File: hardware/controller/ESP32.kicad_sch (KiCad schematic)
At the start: 22 parts, among them J4 Conn_01x04_Pin, Q1 SS8050-G, Q2 SS8050-G, U2 ESP32-S3, Y1 FH4000074Z

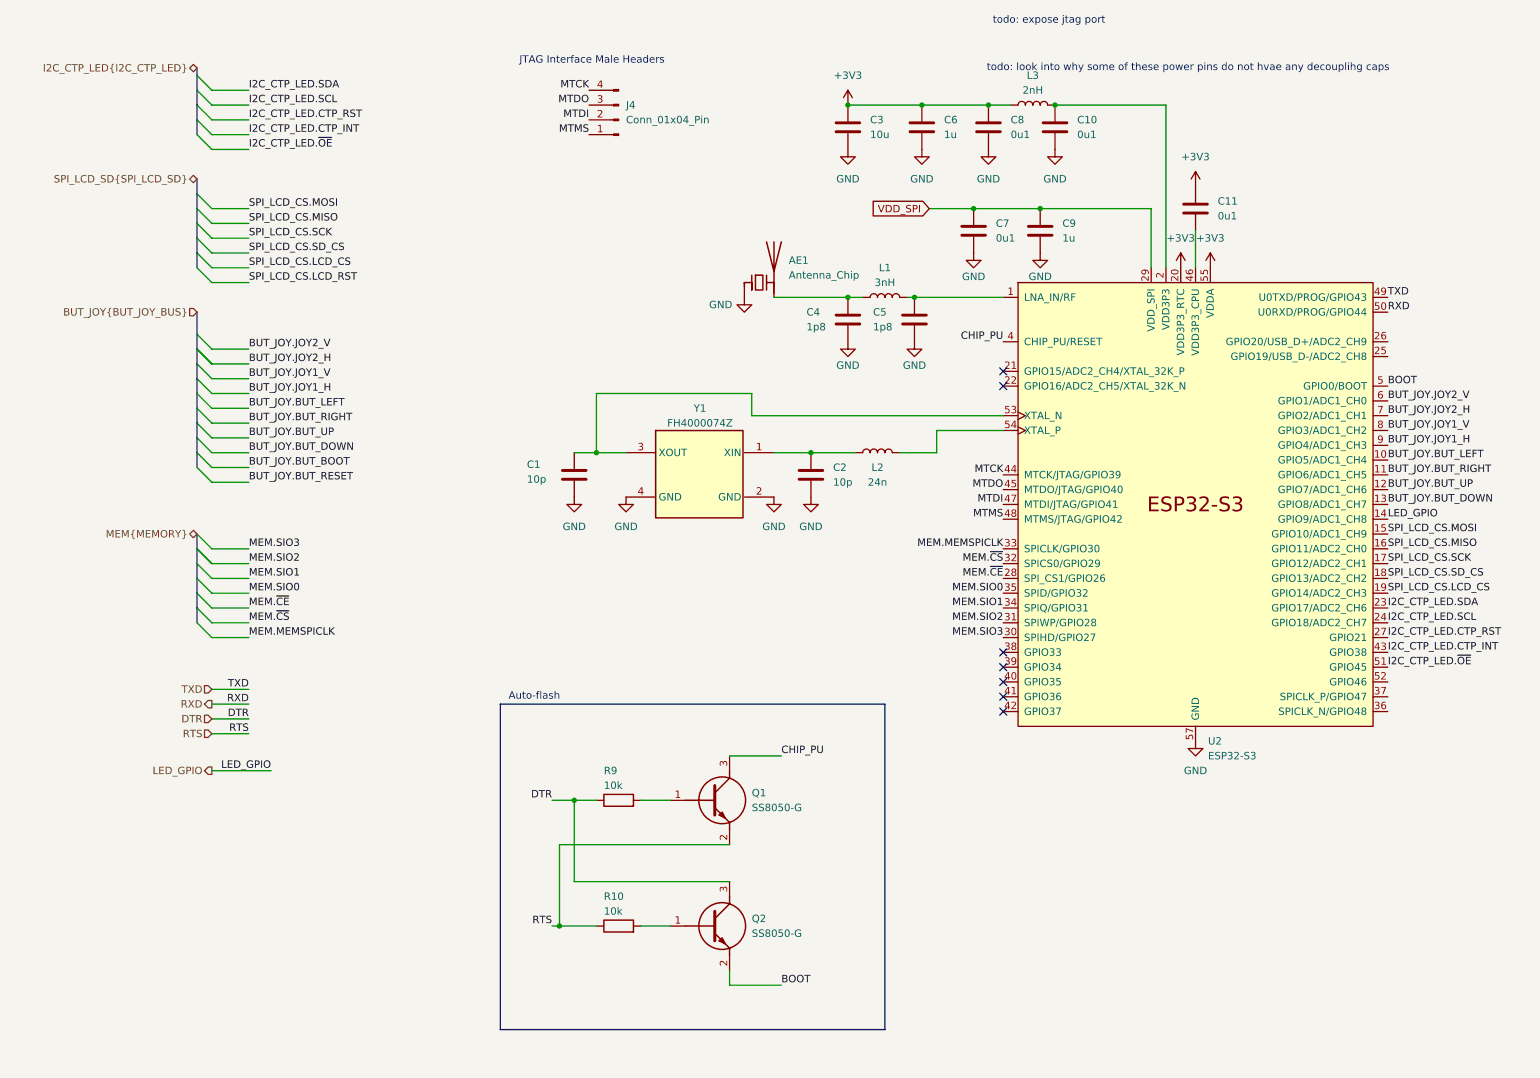
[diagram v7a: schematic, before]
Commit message: modified power circuitry
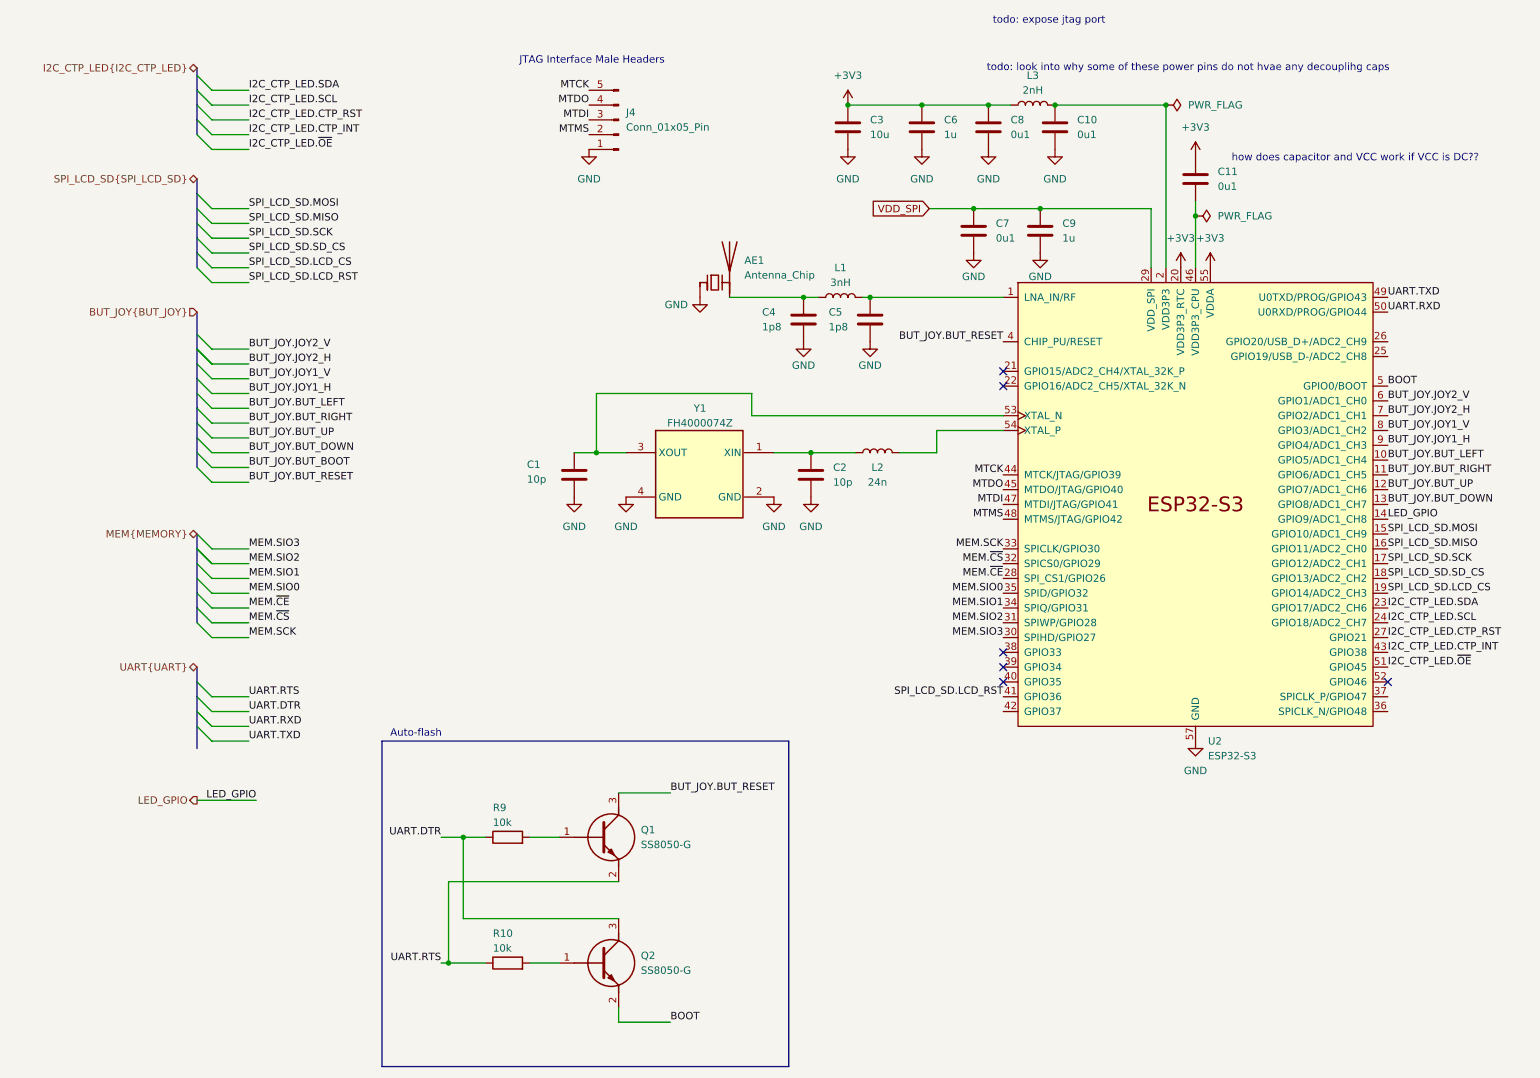
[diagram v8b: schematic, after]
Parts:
- AE1: footprint (none) -> RF_Antenna:Texas_SWRA117D_2.4GHz_Right
- J4: value Conn_01x04_Pin -> Conn_01x05_Pin; footprint (none) -> Connector_PinHeader_2.54mm:PinHeader_1x04_P2.54mm_Vertical; symbol Connector:Conn_01x04_Pin -> Connector:Conn_01x05_Pin
- Q1, Q2: footprint SOT95P240X115-3N -> SamacSys_Parts:SOT95P240X115-3N
- Y1: footprint FH4000074Z -> SamacSys_Parts:FH4000074Z
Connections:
- net CHIP_PU is gone; now on net BUT_JOY.BUT_RESET: Q1.3 (C), U2.4 (CHIP_PU/RESET)
- net GND: now also J4.1 (Pin_1)
- net MTCK: now also J4.5 (Pin_5); no longer J4.4 (Pin_4)
- net MTDI: now also J4.3 (Pin_3); no longer J4.2 (Pin_2)
- net MTDO: now also J4.4 (Pin_4); no longer J4.3 (Pin_3)
- net MTMS: now also J4.2 (Pin_2); no longer J4.1 (Pin_1)
- net SPI_LCD_SD.LCD_RST: now reaches U2.41 (GPIO36)
- net DTR renamed UART.DTR
- net MEM.MEMSPICLK renamed MEM.SCK
- net RTS renamed UART.RTS
- net RXD renamed UART.RXD
- net SPI_LCD_CS.LCD_CS renamed SPI_LCD_SD.LCD_CS
- net SPI_LCD_CS.MISO renamed SPI_LCD_SD.MISO
- net SPI_LCD_CS.MOSI renamed SPI_LCD_SD.MOSI
- net SPI_LCD_CS.SCK renamed SPI_LCD_SD.SCK
- net SPI_LCD_CS.SD_CS renamed SPI_LCD_SD.SD_CS
- net TXD renamed UART.TXD
- no-connect marks 7 -> 6
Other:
- note added: "how does capacitor and VCC work if VCC is DC??"
- moved on the sheet: AE1, C11, C4, C5, L1, Q1, Q2, R10, R9
